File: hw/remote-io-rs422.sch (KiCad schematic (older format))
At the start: 0 parts

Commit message: Added RS-422 Receiver Circuit
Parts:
- added C5: 0.1uF, symbol C
- added R22: 120, symbol R
- added U4: MAX3488, symbol MAX3488
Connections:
- new net +3V3: C5.1, U4.1 (VCC)
- new net GNDD: C5.2, U4.3 (DI), U4.4 (GND)
- new net RS422_GPS: R22.1, U4.8 (A)
- new net RX_GPS: U4.2 (RO)
- new net ~RS422_GPS: R22.2, U4.7 (B)
- no-connect marks 0 -> 2
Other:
- note added: "RS-422 Receiver Circuit"
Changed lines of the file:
@@
 EELAYER 25 0
 EELAYER END
-$Descr A4 11693 8268
+$Descr USLetter 11000 8500
 encoding utf-8
-Sheet 1 1
-Title ""
-Date ""
-Rev ""
-Comp ""
-Comment1 ""
+Sheet 5 5
+Title "RS-422 Level Converter"
+Date "2015-06-16"
+Rev "0"
+Comp "Mirage Manufacturing"
+Comment1 "Designer: Patrick Lloyd"
 Comment2 ""
 Comment3 ""
 Comment4 ""
 $EndDescr
+$Comp
+L MAX3488 U4
+U 1 1 558252CC
+P 4600 3000
+F 0 "U4" H 4400 3400 60  0000 C CNN
+F 1 "MAX3488" H 4550 3300 60  0000 C CNN
+F 2 "" H 4000 3500 60  0000 C CNN
+F 3 "" H 4000 3500 60  0000 C CNN
+	1    4600 3000
+	1    0    0    -1
+$EndComp
+$Comp
+L GNDD #PWR44
+U 1 1 5582541C
+P 4100 3250
+F 0 "#PWR44" H 4100 3000 50  0001 C CNN
+F 1 "GNDD" H 4100 3100 50  0000 C CNN
+F 2 "" H 4100 3250 60  0000 C CNN
+F 3 "" H 4100 3250 60  0000 C CNN
+	1    4100 3250
+	1    0    0    -1
+$EndComp
+NoConn ~ 5100 2900
+NoConn ~ 5100 3000
+$Comp
+L +3.3V #PWR40
+U 1 1 5582543A
+P 4150 2850
+F 0 "#PWR40" H 4150 2700 50  0001 C CNN
+F 1 "+3.3V" H 4150 2990 50  0000 C CNN
+F 2 "" H 4150 2850 60  0000 C CNN
+F 3 "" H 4150 2850 60  0000 C CNN
+	1    4150 2850
+	1    0    0    -1
+$EndComp
+$Comp
+L C C5
+U 1 1 55825450
+P 3150 3050
+F 0 "C5" H 3175 3150 50  0000 L CNN
+F 1 "0.1uF" H 3175 2950 50  0000 L CNN
+F 2 "" H 3188 2900 30  0000 C CNN
+F 3 "" H 3150 3050 60  0000 C CNN
+	1    3150 3050
+	1    0    0    -1
+$EndComp
+$Comp
+L GNDD #PWR43
+U 1 1 55825518
+P 3150 3200
+F 0 "#PWR43" H 3150 2950 50  0001 C CNN
+F 1 "GNDD" H 3150 3050 50  0000 C CNN
+F 2 "" H 3150 3200 60  0000 C CNN
+F 3 "" H 3150 3200 60  0000 C CNN
+	1    3150 3200
+	1    0    0    -1
+$EndComp
+$Comp
+L +3.3V #PWR41
+U 1 1 55825529
+P 3150 2900
+F 0 "#PWR41" H 3150 2750 50  0001 C CNN
+F 1 "+3.3V" H 3150 3040 50  0000 C CNN
+F 2 "" H 3150 2900 60  0000 C CNN
+F 3 "" H 3150 2900 60  0000 C CNN
+	1    3150 2900
+	1    0    0    -1
+$EndComp
+Text HLabel 5500 3300 2    60   Input ~ 0
+~RS422_GPS
+Text HLabel 5500 3000 2    60   Input ~ 0
+RS422_GPS
+Text HLabel 3950 3150 0    60   Output ~ 0
+RX_GPS
+Wire Wire Line
+	5100 3100 5200 3100
+Wire Wire Line
+	5200 3100 5200 3000
+Wire Wire Line
+	5200 3000 5500 3000
+Wire Wire Line
+	5100 3200 5200 3200
+Wire Wire Line
+	5200 3200 5200 3300
+Wire Wire Line
+	5200 3300 5500 3300
+$Comp
+L R R22
+U 1 1 55825A29
+P 5350 3150
+F 0 "R22" V 5430 3150 50  0000 C CNN
+F 1 "120" V 5350 3150 50  0000 C CNN
+F 2 "" V 5280 3150 30  0000 C CNN
+F 3 "" H 5350 3150 30  0000 C CNN
+	1    5350 3150
+	1    0    0    -1
+$EndComp
+Connection ~ 5350 3000
+Connection ~ 5350 3300
+$Comp
+L GNDD #PWR42
+U 1 1 55825C2B
+P 4100 2950
+F 0 "#PWR42" H 4100 2700 50  0001 C CNN
+F 1 "GNDD" H 4100 2800 50  0000 C CNN
+F 2 "" H 4100 2950 60  0000 C CNN
+F 3 "" H 4100 2950 60  0000 C CNN
+	1    4100 2950
+	1    0    0    -1
+$EndComp
+Wire Wire Line
+	4150 3150 3950 3150
+Wire Wire Line
+	4100 2950 4150 2950
+Wire Wire Line
+	4100 3250 4150 3250
+Wire Notes Line
+	3000 2500 3000 3500
+Wire Notes Line
+	3000 3500 6250 3500
+Wire Notes Line
+	6250 3500 6250 2500
+Wire Notes Line
+	6250 2500 3000 2500
+Text Notes 3000 2500 0    60   ~ 0
+RS-422 Receiver Circuit
 $EndSCHEMATC

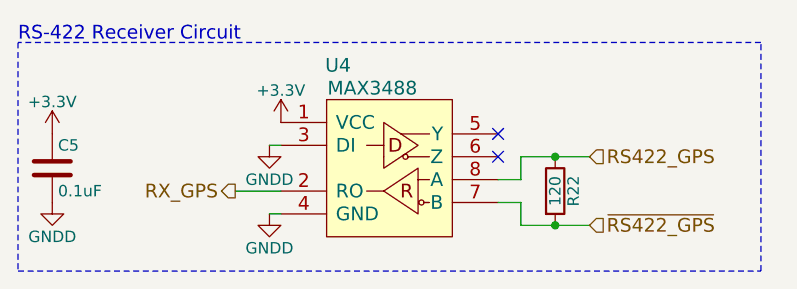
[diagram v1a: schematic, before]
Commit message: Matched all footprints to schem and created kicad_pcb file
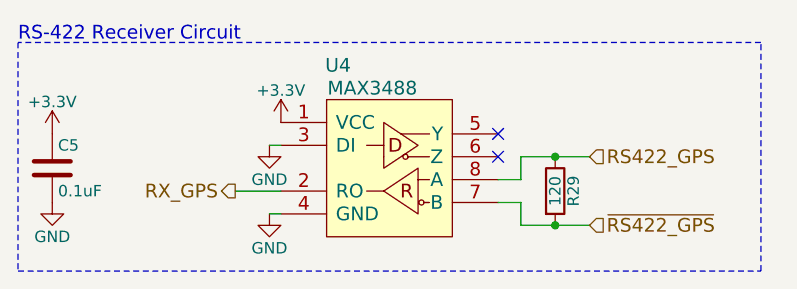
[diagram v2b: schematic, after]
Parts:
- C5: footprint (none) -> Capacitors_SMD:C_0805_HandSoldering
- R29: renamed from R22; footprint (none) -> Resistors_SMD:R_0805_HandSoldering
- U4: footprint (none) -> Housings_SOIC:SOIC-8_3.9x4.9mm_Pitch1.27mm
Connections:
- net GNDD renamed GND
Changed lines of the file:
@@
 F 0 "U4" H 4400 3400 60  0000 C CNN
 F 1 "MAX3488" H 4550 3300 60  0000 C CNN
-F 2 "" H 4000 3500 60  0000 C CNN
+F 2 "Housings_SOIC:SOIC-8_3.9x4.9mm_Pitch1.27mm" H 4000 3500 60  0001 C CNN
 F 3 "" H 4000 3500 60  0000 C CNN
 	1    4600 3000
-	1    0    0    -1
-$EndComp
-$Comp
-L GNDD #PWR44
-U 1 1 5582541C
-P 4100 3250
-F 0 "#PWR44" H 4100 3000 50  0001 C CNN
-F 1 "GNDD" H 4100 3100 50  0000 C CNN
-F 2 "" H 4100 3250 60  0000 C CNN
-F 3 "" H 4100 3250 60  0000 C CNN
-	1    4100 3250
 	1    0    0    -1
 $EndComp
@@
 NoConn ~ 5100 3000
 $Comp
-L +3.3V #PWR40
+L +3.3V #PWR051
 U 1 1 5582543A
 P 4150 2850
-F 0 "#PWR40" H 4150 2700 50  0001 C CNN
+F 0 "#PWR051" H 4150 2700 50  0001 C CNN
 F 1 "+3.3V" H 4150 2990 50  0000 C CNN
 F 2 "" H 4150 2850 60  0000 C CNN
@@
 F 0 "C5" H 3175 3150 50  0000 L CNN
 F 1 "0.1uF" H 3175 2950 50  0000 L CNN
-F 2 "" H 3188 2900 30  0000 C CNN
+F 2 "Capacitors_SMD:C_0805_HandSoldering" H 3188 2900 30  0001 C CNN
 F 3 "" H 3150 3050 60  0000 C CNN
 	1    3150 3050
@@
 $EndComp
 $Comp
-L GNDD #PWR43
-U 1 1 55825518
-P 3150 3200
-F 0 "#PWR43" H 3150 2950 50  0001 C CNN
-F 1 "GNDD" H 3150 3050 50  0000 C CNN
-F 2 "" H 3150 3200 60  0000 C CNN
-F 3 "" H 3150 3200 60  0000 C CNN
-	1    3150 3200
-	1    0    0    -1
-$EndComp
-$Comp
-L +3.3V #PWR41
+L +3.3V #PWR052
 U 1 1 55825529
 P 3150 2900
-F 0 "#PWR41" H 3150 2750 50  0001 C CNN
+F 0 "#PWR052" H 3150 2750 50  0001 C CNN
 F 1 "+3.3V" H 3150 3040 50  0000 C CNN
 F 2 "" H 3150 2900 60  0000 C CNN
@@
 	5200 3300 5500 3300
 $Comp
-L R R22
+L R R29
 U 1 1 55825A29
 P 5350 3150
-F 0 "R22" V 5430 3150 50  0000 C CNN
+F 0 "R29" V 5430 3150 50  0000 C CNN
 F 1 "120" V 5350 3150 50  0000 C CNN
-F 2 "" V 5280 3150 30  0000 C CNN
+F 2 "Resistors_SMD:R_0805_HandSoldering" V 5280 3150 30  0001 C CNN
 F 3 "" H 5350 3150 30  0000 C CNN
 	1    5350 3150
@@
 Connection ~ 5350 3000
 Connection ~ 5350 3300
-$Comp
-L GNDD #PWR42
-U 1 1 55825C2B
-P 4100 2950
-F 0 "#PWR42" H 4100 2700 50  0001 C CNN
-F 1 "GNDD" H 4100 2800 50  0000 C CNN
-F 2 "" H 4100 2950 60  0000 C CNN
-F 3 "" H 4100 2950 60  0000 C CNN
-	1    4100 2950
-	1    0    0    -1
-$EndComp
 Wire Wire Line
 	4150 3150 3950 3150
@@
 Text Notes 3000 2500 0    60   ~ 0
 RS-422 Receiver Circuit
+$Comp
+L GND #PWR053
+U 1 1 5582A0AF
+P 3150 3200
+F 0 "#PWR053" H 3150 2950 50  0001 C CNN
+F 1 "GND" H 3150 3050 50  0000 C CNN
+F 2 "" H 3150 3200 60  0000 C CNN
+F 3 "" H 3150 3200 60  0000 C CNN
+	1    3150 3200
+	1    0    0    -1
+$EndComp
+$Comp
+L GND #PWR054
+U 1 1 5582A0F5
+P 4100 3250
+F 0 "#PWR054" H 4100 3000 50  0001 C CNN
+F 1 "GND" H 4100 3100 50  0000 C CNN
+F 2 "" H 4100 3250 60  0000 C CNN
+F 3 "" H 4100 3250 60  0000 C CNN
+	1    4100 3250
+	1    0    0    -1
+$EndComp
+$Comp
+L GND #PWR055
+U 1 1 5582A10C
+P 4100 2950
+F 0 "#PWR055" H 4100 2700 50  0001 C CNN
+F 1 "GND" H 4100 2800 50  0000 C CNN
+F 2 "" H 4100 2950 60  0000 C CNN
+F 3 "" H 4100 2950 60  0000 C CNN
+	1    4100 2950
+	1    0    0    -1
+$EndComp
 $EndSCHEMATC

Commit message: added CAN power, controller, and transceiver to schem and updated PCB
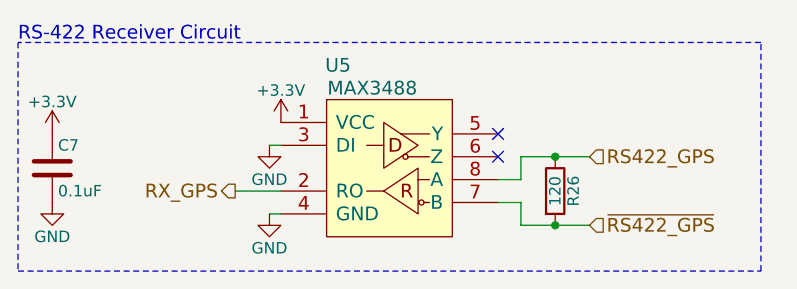
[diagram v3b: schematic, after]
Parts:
- renumbered C5 to C7, R29 to R26, U4 to U5
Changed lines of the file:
@@
 $Descr USLetter 11000 8500
 encoding utf-8
-Sheet 5 5
+Sheet 5 6
 Title "RS-422 Level Converter"
 Date "2015-06-16"
@@
 $EndDescr
 $Comp
-L MAX3488 U4
+L MAX3488 U5
 U 1 1 558252CC
 P 4600 3000
-F 0 "U4" H 4400 3400 60  0000 C CNN
+F 0 "U5" H 4400 3400 60  0000 C CNN
 F 1 "MAX3488" H 4550 3300 60  0000 C CNN
 F 2 "Housings_SOIC:SOIC-8_3.9x4.9mm_Pitch1.27mm" H 4000 3500 60  0001 C CNN
@@
 NoConn ~ 5100 3000
 $Comp
-L +3.3V #PWR051
+L +3.3V #PWR057
 U 1 1 5582543A
 P 4150 2850
-F 0 "#PWR051" H 4150 2700 50  0001 C CNN
+F 0 "#PWR057" H 4150 2700 50  0001 C CNN
 F 1 "+3.3V" H 4150 2990 50  0000 C CNN
 F 2 "" H 4150 2850 60  0000 C CNN
@@
 $EndComp
 $Comp
-L C C5
+L C C7
 U 1 1 55825450
 P 3150 3050
-F 0 "C5" H 3175 3150 50  0000 L CNN
+F 0 "C7" H 3175 3150 50  0000 L CNN
 F 1 "0.1uF" H 3175 2950 50  0000 L CNN
 F 2 "Capacitors_SMD:C_0805_HandSoldering" H 3188 2900 30  0001 C CNN
@@
 $EndComp
 $Comp
-L +3.3V #PWR052
+L +3.3V #PWR058
 U 1 1 55825529
 P 3150 2900
-F 0 "#PWR052" H 3150 2750 50  0001 C CNN
+F 0 "#PWR058" H 3150 2750 50  0001 C CNN
 F 1 "+3.3V" H 3150 3040 50  0000 C CNN
 F 2 "" H 3150 2900 60  0000 C CNN
@@
 	5200 3300 5500 3300
 $Comp
-L R R29
+L R R26
 U 1 1 55825A29
 P 5350 3150
-F 0 "R29" V 5430 3150 50  0000 C CNN
+F 0 "R26" V 5430 3150 50  0000 C CNN
 F 1 "120" V 5350 3150 50  0000 C CNN
 F 2 "Resistors_SMD:R_0805_HandSoldering" V 5280 3150 30  0001 C CNN
@@
 RS-422 Receiver Circuit
 $Comp
-L GND #PWR053
+L GND #PWR059
 U 1 1 5582A0AF
 P 3150 3200
-F 0 "#PWR053" H 3150 2950 50  0001 C CNN
+F 0 "#PWR059" H 3150 2950 50  0001 C CNN
 F 1 "GND" H 3150 3050 50  0000 C CNN
 F 2 "" H 3150 3200 60  0000 C CNN
@@
 $EndComp
 $Comp
-L GND #PWR054
+L GND #PWR060
 U 1 1 5582A0F5
 P 4100 3250
-F 0 "#PWR054" H 4100 3000 50  0001 C CNN
+F 0 "#PWR060" H 4100 3000 50  0001 C CNN
 F 1 "GND" H 4100 3100 50  0000 C CNN
 F 2 "" H 4100 3250 60  0000 C CNN
@@
 $EndComp
 $Comp
-L GND #PWR055
+L GND #PWR061
 U 1 1 5582A10C
 P 4100 2950
-F 0 "#PWR055" H 4100 2700 50  0001 C CNN
+F 0 "#PWR061" H 4100 2700 50  0001 C CNN
 F 1 "GND" H 4100 2800 50  0000 C CNN
 F 2 "" H 4100 2950 60  0000 C CNN

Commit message: Started fucking aroond with pcb layout. Power is tricky...
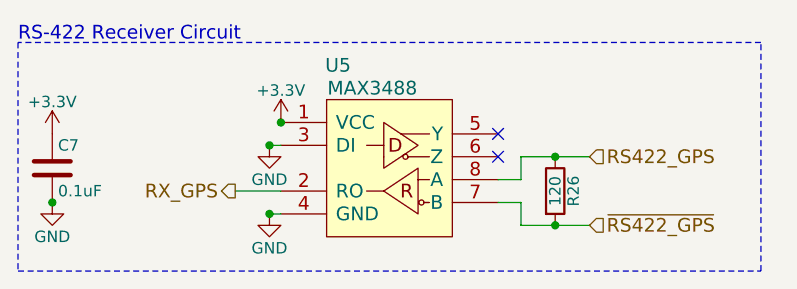
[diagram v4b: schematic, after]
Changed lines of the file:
@@
 NoConn ~ 5100 3000
 $Comp
-L +3.3V #PWR057
+L +3.3V #PWR054
 U 1 1 5582543A
 P 4150 2850
-F 0 "#PWR057" H 4150 2700 50  0001 C CNN
+F 0 "#PWR054" H 4150 2700 50  0001 C CNN
 F 1 "+3.3V" H 4150 2990 50  0000 C CNN
 F 2 "" H 4150 2850 60  0000 C CNN
@@
 $EndComp
 $Comp
-L +3.3V #PWR058
+L +3.3V #PWR055
 U 1 1 55825529
 P 3150 2900
-F 0 "#PWR058" H 3150 2750 50  0001 C CNN
+F 0 "#PWR055" H 3150 2750 50  0001 C CNN
 F 1 "+3.3V" H 3150 3040 50  0000 C CNN
 F 2 "" H 3150 2900 60  0000 C CNN
@@
 RS-422 Receiver Circuit
 $Comp
-L GND #PWR059
+L GND #PWR056
 U 1 1 5582A0AF
 P 3150 3200
-F 0 "#PWR059" H 3150 2950 50  0001 C CNN
+F 0 "#PWR056" H 3150 2950 50  0001 C CNN
 F 1 "GND" H 3150 3050 50  0000 C CNN
 F 2 "" H 3150 3200 60  0000 C CNN
@@
 $EndComp
 $Comp
-L GND #PWR060
+L GND #PWR057
 U 1 1 5582A0F5
 P 4100 3250
-F 0 "#PWR060" H 4100 3000 50  0001 C CNN
+F 0 "#PWR057" H 4100 3000 50  0001 C CNN
 F 1 "GND" H 4100 3100 50  0000 C CNN
 F 2 "" H 4100 3250 60  0000 C CNN
@@
 $EndComp
 $Comp
-L GND #PWR061
+L GND #PWR058
 U 1 1 5582A10C
 P 4100 2950
-F 0 "#PWR061" H 4100 2700 50  0001 C CNN
+F 0 "#PWR058" H 4100 2700 50  0001 C CNN
 F 1 "GND" H 4100 2800 50  0000 C CNN
 F 2 "" H 4100 2950 60  0000 C CNN
@@
 	1    0    0    -1
 $EndComp
+Connection ~ 3150 3200
+Connection ~ 4100 3250
+Connection ~ 4100 2950
+Connection ~ 4150 2850
 $EndSCHEMATC
